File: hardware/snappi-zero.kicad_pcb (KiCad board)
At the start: 2 copper layers, 0 parts

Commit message: Place and route initial board.
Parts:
- added D1: A, LEDs:LED_1206, F.Cu at (210.0, 86.0)
- added D2: B, LEDs:LED_1206, F.Cu at (210.0, 90.5)
- added D3: C, LEDs:LED_1206, F.Cu at (210.0, 95.0)
- added G***: LOGO, CrumpPrintSymbols:Symbol_OSHW-Logo_12.5mm_NoText_Silkscreen, B.Cu at (202.0, 87.0)
- added G***: LOGO, ProjectSpecific:snappi-zero-logo, F.Cu at (199.5, 89.0)
- added P1: CONN_02X20, CrumpPrints:Raspberry_Pi_Zero, F.Cu at (148.5, 105.0)
- added R1: 10k, Resistors_SMD:R_0805_HandSoldering, F.Cu at (162.6, 101.6)
- added R2: 1k, Resistors_SMD:R_0805_HandSoldering, F.Cu at (200.0, 101.0)
- added R3: 1k, Resistors_SMD:R_0805_HandSoldering, F.Cu at (200.0, 103.5)
- added R4: 1k, Resistors_SMD:R_0805_HandSoldering, F.Cu at (200.0, 106.0)
- added U1: RF200, CrumpPrints:RF200_nosilk, F.Cu at (174.5, 95.0)
- added U2: SM220UF1, CrumpPrints:SM200_nosilk, F.Cu at (176.0, 93.5)
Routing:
- net GPIO_17: track 0.00 -> 64.5 mm, vias 0 -> 3
- net LED_C: track 0.00 -> 47.2 mm
- net LED_B: track 0.00 -> 38.6 mm
- net 3v3: track 0.00 -> 32.6 mm
- net LED_A: track 0.00 -> 32.3 mm
- net PI_TX: track 0.00 -> 32.0 mm, vias 0 -> 4
- net PI_RX: track 0.00 -> 27.0 mm
- net Net-(D1-Pad2): track 0.00 -> 17.9 mm
- net Net-(D2-Pad2): track 0.00 -> 16.3 mm
- net Net-(D3-Pad2): track 0.00 -> 15.7 mm
- net GND: track 0.00 -> 3.53 mm, vias 0 -> 2
- added copper zone on B.Cu, net GND
- added copper zone on F.Cu, net GND
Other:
- board outline added: 65 x 33 mm
- net class Default: clearance 0.254 -> 0.2032
- net class Thin added: clearance 0.1524, trace_width 0.2032, via_dia 0.889, via_drill 0.635
- rule trace_clearance: 0.254 -> 0.2032
- rule trace_min: 0.254 -> 0.1524
- board text added: "CC-BY-SA 4.0 @tylercrumpton"
- board text added: "SNAP Reset (Active Low): - Raspberry Pi BCM17 LED A: - RF GPIO_2 - SM GPIO_D3 LED B: - RF GPIO_1 - SM GPIO_D2 LED C: - RF GPIO_0 - SM GPIO_D1"
- board text added: "v1.0"

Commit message: Add TC logo and finalize PCB.
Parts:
- added svg2mod: G***, CrumpPrintSymbols:tc_30mm, F.Cu at (152.5, 85.5)
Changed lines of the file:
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@@
     (links 31)
     (no_connects 0)
-    (area 148.449999 74.949999 213.550001 108.050001)
+    (area 147.289372 73.0218 215.679391 116.278201)
     (thickness 1.6)
     (drawings 30)
     (tracks 106)
     (zones 0)
-    (modules 12)
+    (modules 13)
     (nets 92)
   )
@@
       (outputformat 1)
       (mirror false)
-      (drillshape 1)
+      (drillshape 0)
       (scaleselection 1)
       (outputdirectory ""))
@@
       (xy 2.253444 -4.352498)) (layer F.SilkS) (width 0.01))
   )
+  (module CrumpPrintSymbols:tc_30mm (layer F.Cu)
+    (at 152.5 85.5)
+    (descr "Imported from ../../../Dropbox/Vector Images/Other/tylercrumpton/tc.svg")
+    (tags svg2mod)
+    (attr smd)
+    (fp_text reference svg2mod (at 0 -5.231772) (layer F.SilkS) hide
+      (effects (font (thickness 0.3048)))
+    )
+    (fp_text value G*** (at 0 5.231772) (layer F.SilkS) hide
+      (effects (font (thickness 0.3048)))
+    )
+    (fp_poly (pts (xy 2.193664 1.877434) (xy 2.193664 -1.877434) (xy -2.193661 -1.877434) (xy -2.193661 1.877434)
+      (xy -0.80057 1.877434) (xy -0.80057 2.183772) (xy -2.499999 2.183772) (xy -2.499999 -2.183772)
+      (xy 2.499999 -2.183772) (xy 2.499999 2.183772) (xy 0.800528 2.183772) (xy 0.800528 1.877434)
+      (xy 2.193664 1.877434)) (layer F.SilkS) (width 0))
+    (fp_poly (pts (xy -0.686701 -0.454978) (xy -0.686701 0.8898) (xy -1.058682 0.8898) (xy -1.058682 -0.454978)
+      (xy -1.530792 -0.454978) (xy -1.530792 -0.776852) (xy -0.21459 -0.776852) (xy -0.21459 -0.454978)
+      (xy -0.686701 -0.454978)) (layer F.SilkS) (width 0))
+    (fp_poly (pts (xy 0.822581 0.56075) (xy 1.071754 0.506517) (xy 1.270841 0.343775) (xy 1.509259 0.589327)
+      (xy 1.308846 0.766865) (xy 1.08591 0.873352) (xy 0.84048 0.908837) (xy 0.598838 0.881819)
+      (xy 0.387421 0.80076) (xy 0.20623 0.665649) (xy 0.067795 0.489341) (xy -0.015267 0.284685)
+      (xy -0.042954 0.051661) (xy -0.01474 -0.181871) (xy 0.069908 -0.388124) (xy 0.211 -0.567098)
+      (xy 0.392861 -0.704846) (xy 0.59989 -0.787502) (xy 0.832078 -0.815056) (xy 1.09064 -0.780353)
+      (xy 1.31955 -0.676242) (xy 1.518799 -0.502723) (xy 1.287514 -0.240411) (xy 1.089604 -0.404947)
+      (xy 0.848795 -0.459792) (xy 0.654139 -0.425521) (xy 0.489942 -0.322684) (xy 0.378167 -0.161726)
+      (xy 0.340931 0.04689) (xy 0.376094 0.256414) (xy 0.481628 0.420053) (xy 0.637187 0.525587)
+      (xy 0.822581 0.56075)) (layer F.SilkS) (width 0))
+  )
   (gr_text "SNAP Reset (Active Low): \n - Raspberry Pi BCM17\nLED A:\n - RF GPIO_2\n - SM GPIO_D3\nLED B:\n - RF GPIO_1\n - SM GPIO_D2\nLED C:\n - RF GPIO_0\n - SM GPIO_D1" (at 184.5 95.5) (layer B.SilkS)

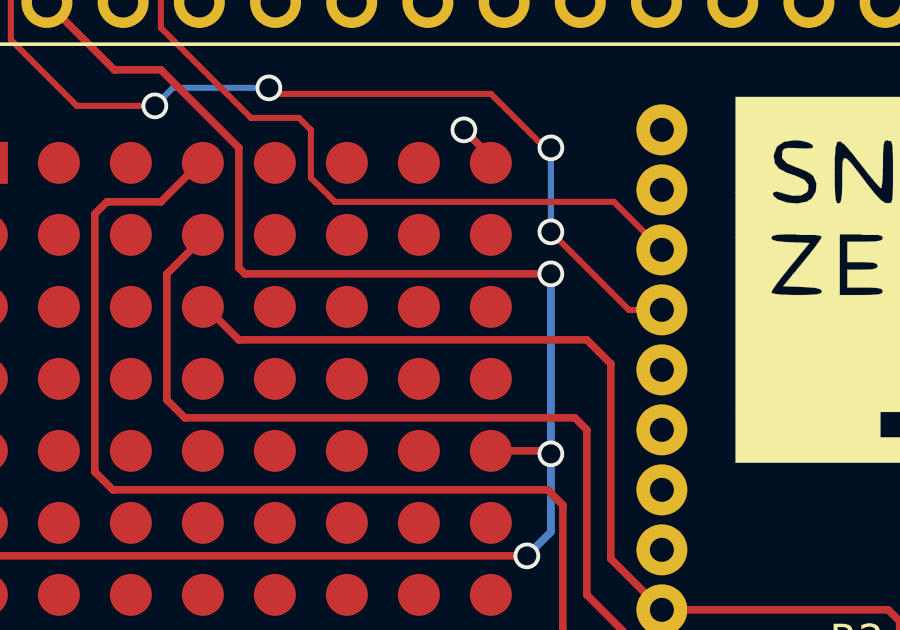
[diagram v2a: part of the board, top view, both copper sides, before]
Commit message: Fix missing TX/RX pins on SM modules.
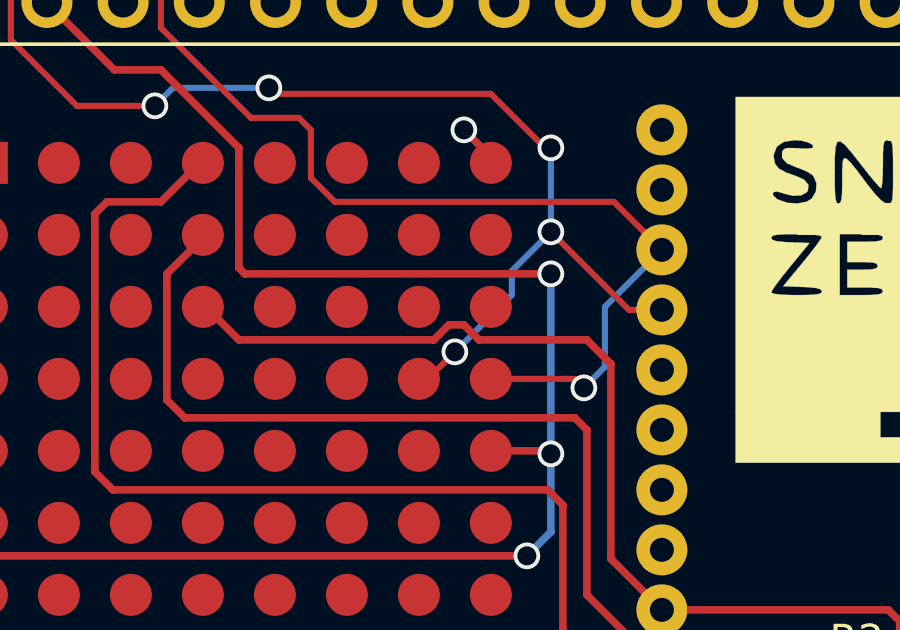
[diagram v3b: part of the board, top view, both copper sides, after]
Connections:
- P1 pad 13: Net-(P1-Pad13) -> (no net)
- P1 pad 14: Net-(P1-Pad14) -> (no net)
- P1 pad 15: Net-(P1-Pad15) -> (no net)
- P1 pad 16: Net-(P1-Pad16) -> (no net)
- P1 pad 17: Net-(P1-Pad17) -> (no net)
- P1 pad 18: Net-(P1-Pad18) -> (no net)
- P1 pad 19: Net-(P1-Pad19) -> (no net)
- P1 pad 2: Net-(P1-Pad2) -> (no net)
- P1 pad 20: Net-(P1-Pad20) -> (no net)
- P1 pad 21: Net-(P1-Pad21) -> (no net)
- P1 pad 22: Net-(P1-Pad22) -> (no net)
- P1 pad 23: Net-(P1-Pad23) -> (no net)
- P1 pad 24: Net-(P1-Pad24) -> (no net)
- P1 pad 25: Net-(P1-Pad25) -> (no net)
- P1 pad 26: Net-(P1-Pad26) -> (no net)
- P1 pad 27: Net-(P1-Pad27) -> (no net)
- P1 pad 28: Net-(P1-Pad28) -> (no net)
- P1 pad 29: Net-(P1-Pad29) -> (no net)
- P1 pad 3: Net-(P1-Pad3) -> (no net)
- P1 pad 30: Net-(P1-Pad30) -> (no net)
- P1 pad 31: Net-(P1-Pad31) -> (no net)
- P1 pad 32: Net-(P1-Pad32) -> (no net)
- P1 pad 33: Net-(P1-Pad33) -> (no net)
- P1 pad 34: Net-(P1-Pad34) -> (no net)
- P1 pad 35: Net-(P1-Pad35) -> (no net)
- P1 pad 36: Net-(P1-Pad36) -> (no net)
- P1 pad 37: Net-(P1-Pad37) -> (no net)
- P1 pad 38: Net-(P1-Pad38) -> (no net)
- P1 pad 39: Net-(P1-Pad39) -> (no net)
- P1 pad 4: Net-(P1-Pad4) -> (no net)
- P1 pad 40: Net-(P1-Pad40) -> (no net)
- P1 pad 5: Net-(P1-Pad5) -> (no net)
- P1 pad 6: Net-(P1-Pad6) -> (no net)
- P1 pad 7: Net-(P1-Pad7) -> (no net)
- P1 pad 8: Net-(P1-Pad8) -> (no net)
- U1 pad 11: Net-(U1-Pad11) -> (no net)
- U1 pad 12: Net-(U1-Pad12) -> (no net)
- U1 pad 13: Net-(U1-Pad13) -> (no net)
- U1 pad 14: Net-(U1-Pad14) -> (no net)
- U1 pad 15: Net-(U1-Pad15) -> (no net)
- U1 pad 16: Net-(U1-Pad16) -> (no net)
- U1 pad 17: Net-(U1-Pad17) -> (no net)
- U1 pad 18: Net-(U1-Pad18) -> (no net)
- U1 pad 19: Net-(U1-Pad19) -> (no net)
- U1 pad 20: Net-(U1-Pad20) -> (no net)
- U1 pad 22: Net-(U1-Pad22) -> (no net)
- U1 pad 5: Net-(U1-Pad5) -> (no net)
- U1 pad 6: Net-(U1-Pad6) -> (no net)
- U1 pad 7: Net-(U1-Pad7) -> (no net)
- U1 pad 8: Net-(U1-Pad8) -> (no net)
- U2 pad A4: Net-(U2-PadA4) -> (no net)
- U2 pad A5: Net-(U2-PadA5) -> (no net)
- U2 pad A6: Net-(U2-PadA6) -> (no net)
- U2 pad A7: Net-(U2-PadA7) -> (no net)
- U2 pad B1: Net-(U2-PadB1) -> (no net)
- U2 pad B2: Net-(U2-PadB2) -> (no net)
- U2 pad B3: Net-(U2-PadB3) -> (no net)
- U2 pad B4: Net-(U2-PadB4) -> (no net)
- U2 pad B6: Net-(U2-PadB6) -> (no net)
- U2 pad B7: Net-(U2-PadB7) -> (no net)
- U2 pad C1: Net-(U2-PadC1) -> (no net)
- U2 pad C2: Net-(U2-PadC2) -> (no net)
- U2 pad C3: Net-(U2-PadC3) -> (no net)
- U2 pad C4: Net-(U2-PadC4) -> (no net)
- U2 pad C5: Net-(U2-PadC5) -> (no net)
- U2 pad E1: Net-(U2-PadE1) -> (no net)
- U2 pad E2: Net-(U2-PadE2) -> (no net)
- U2 pad E3: Net-(U2-PadE3) -> (no net)
- U2 pad F1: Net-(U2-PadF1) -> (no net)
- U2 pad F2: Net-(U2-PadF2) -> (no net)
- U2 pad F3: Net-(U2-PadF3) -> (no net)
- U2 pad F4: Net-(U2-PadF4) -> (no net)
- U2 pad G1: Net-(U2-PadG1) -> (no net)
- U2 pad G2: Net-(U2-PadG2) -> (no net)
- U2 pad G3: Net-(U2-PadG3) -> (no net)
- U2 pad G4: Net-(U2-PadG4) -> PI_TX
- U2 pad G5: Net-(U2-PadG5) -> (no net)
- U2 pad H2: Net-(U2-PadH2) -> (no net)
- U2 pad H3: Net-(U2-PadH3) -> (no net)
- U2 pad H4: Net-(U2-PadH4) -> PI_RX
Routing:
- net PI_RX: track 27.0 -> 35.9 mm, vias 0 -> 1
- net PI_TX: track 32.0 -> 38.9 mm, vias 4 -> 5

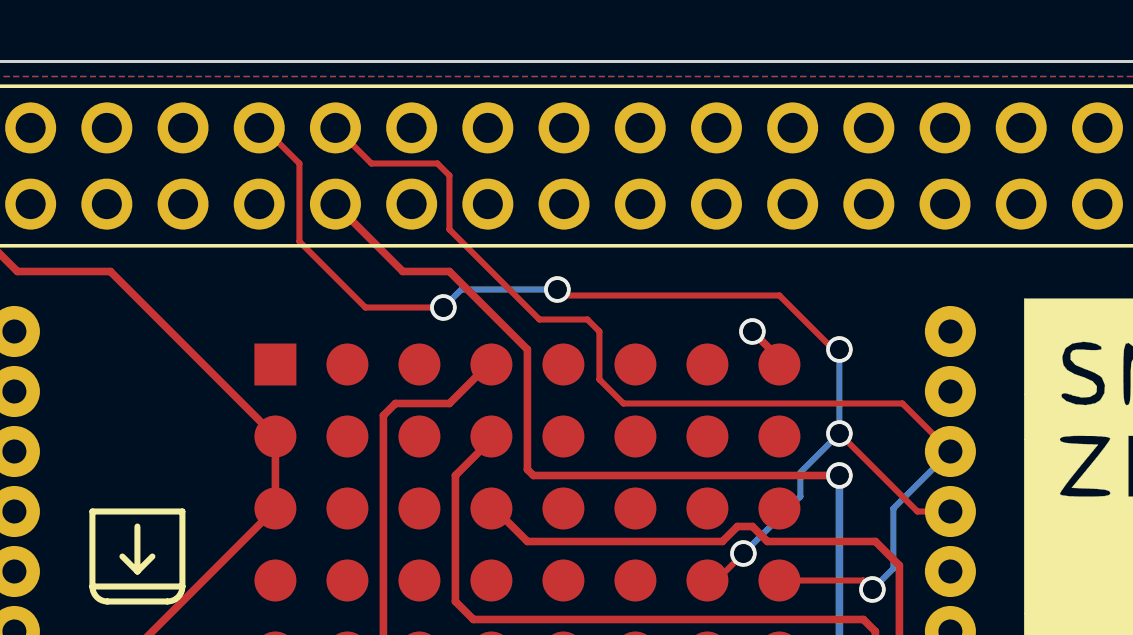
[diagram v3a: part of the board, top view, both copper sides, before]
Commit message: Fix Pi RX/TX pins.
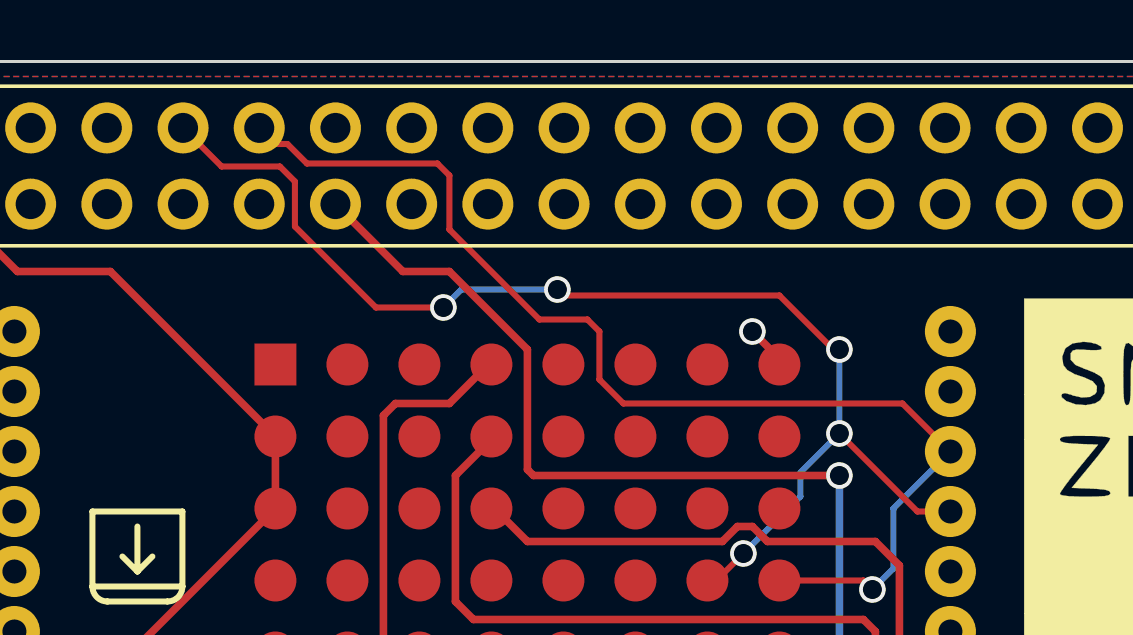
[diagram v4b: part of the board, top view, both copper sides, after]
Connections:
- P1 pad 10: PI_TX -> PI_RX
- P1 pad 12: PI_RX -> (no net)
- P1 pad 8: (no net) -> PI_TX
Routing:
- net PI_RX: track 35.9 -> 38.4 mm
- net PI_TX: track 38.9 -> 40.8 mm
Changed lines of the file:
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@@
     (thickness 1.6)
     (drawings 30)
-    (tracks 122)
+    (tracks 124)
     (zones 0)
     (modules 13)
@@
     (pad 6 thru_hole oval (at 13.48 -27.79 90) (size 1.7 1.7) (drill 1) (layers *.Cu *.Mask))
     (pad 7 thru_hole oval (at 16.02 -25.25 90) (size 1.7 1.7) (drill 1) (layers *.Cu *.Mask))
-    (pad 8 thru_hole oval (at 16.02 -27.79 90) (size 1.7 1.7) (drill 1) (layers *.Cu *.Mask))
+    (pad 8 thru_hole oval (at 16.02 -27.79 90) (size 1.7 1.7) (drill 1) (layers *.Cu *.Mask)
+      (net 6 PI_TX))
     (pad 9 thru_hole oval (at 18.56 -25.25 90) (size 1.7 1.7) (drill 1) (layers *.Cu *.Mask)
       (net 2 GND))
     (pad 10 thru_hole oval (at 18.56 -27.79 90) (size 1.7 1.7) (drill 1) (layers *.Cu *.Mask)
-      (net 6 PI_TX))
+      (net 8 PI_RX))
     (pad 11 thru_hole oval (at 21.1 -25.25 90) (size 1.7 1.7) (drill 1) (layers *.Cu *.Mask)
       (net 7 GPIO_17))
-    (pad 12 thru_hole oval (at 21.1 -27.79 90) (size 1.7 1.7) (drill 1) (layers *.Cu *.Mask)
-      (net 8 PI_RX))
+    (pad 12 thru_hole oval (at 21.1 -27.79 90) (size 1.7 1.7) (drill 1) (layers *.Cu *.Mask))
     (pad 13 thru_hole oval (at 23.64 -25.25 90) (size 1.7 1.7) (drill 1) (layers *.Cu *.Mask))
     (pad 14 thru_hole oval (at 23.64 -27.79 90) (size 1.7 1.7) (drill 1) (layers *.Cu *.Mask))
@@
   (segment (start 158.9 100) (end 162.31 100) (width 0.254) (layer F.Cu) (net 5))
   (segment (start 162.31 100) (end 162.56 100.25) (width 0.254) (layer F.Cu) (net 5))
-  (segment (start 185.1 88.7) (end 186.4 87.4) (width 0.2032) (layer B.Cu) (net 6))
-  (segment (start 185.1 89.5) (end 185.1 88.7) (width 0.2032) (layer B.Cu) (net 6))
-  (segment (start 183.2 91.4) (end 185.1 89.5) (width 0.2032) (layer B.Cu) (net 6))
-  (via (at 183.2 91.4) (size 0.889) (drill 0.635) (layers F.Cu B.Cu) (net 6))
-  (segment (start 182.3 92.3) (end 183.2 91.4) (width 0.2032) (layer F.Cu) (net 6))
-  (segment (start 182 92.3) (end 182.3 92.3) (width 0.2032) (layer F.Cu) (net 6))
-  (segment (start 167.0611 77.2136) (end 167.2136 77.2136) (width 0.2032) (layer F.Cu) (net 6))
-  (segment (start 167.2136 77.2136) (end 168.4 78.4) (width 0.2032) (layer F.Cu) (net 6))
-  (segment (start 168.4 78.4) (end 168.4 81) (width 0.2032) (layer F.Cu) (net 6))
-  (segment (start 168.4 81) (end 170.6 83.2) (width 0.2032) (layer F.Cu) (net 6))
-  (segment (start 170.6 83.2) (end 173.2 83.2) (width 0.2032) (layer F.Cu) (net 6))
+  (segment (start 173.2 83.2) (end 170.95 83.2) (width 0.2032) (layer F.Cu) (net 6))
+  (segment (start 186.4 87.4) (end 186.4 84.6) (width 0.2032) (layer B.Cu) (net 6))
+  (via (at 186.4 84.6) (size 0.889) (drill 0.635) (layers F.Cu B.Cu) (net 6))
+  (segment (start 184.4 82.8) (end 186.2 84.6) (width 0.2032) (layer F.Cu) (net 6))
   (via (at 173.2 83.2) (size 0.889) (drill 0.635) (layers F.Cu B.Cu) (net 6))
   (segment (start 173.2 83.2) (end 173.8 82.6) (width 0.2032) (layer B.Cu) (net 6))
@@
   (segment (start 177 82.6) (end 177.2 82.8) (width 0.2032) (layer F.Cu) (net 6))
   (segment (start 177.2 82.8) (end 184.4 82.8) (width 0.2032) (layer F.Cu) (net 6))
-  (segment (start 184.4 82.8) (end 186.2 84.6) (width 0.2032) (layer F.Cu) (net 6))
   (segment (start 186.2 84.6) (end 186.4 84.6) (width 0.2032) (layer F.Cu) (net 6))
-  (via (at 186.4 84.6) (size 0.889) (drill 0.635) (layers F.Cu B.Cu) (net 6))
-  (segment (start 186.4 84.6) (end 186.4 87.4) (width 0.2032) (layer B.Cu) (net 6))
+  (segment (start 165.8075 78.5) (end 164.5211 77.2136) (width 0.2032) (layer F.Cu) (net 6))
+  (segment (start 167.75 78.5) (end 165.8075 78.5) (width 0.2032) (layer F.Cu) (net 6))
+  (segment (start 168.25 79) (end 167.75 78.5) (width 0.2032) (layer F.Cu) (net 6))
+  (segment (start 168.25 80.5) (end 168.25 79) (width 0.2032) (layer F.Cu) (net 6))
+  (segment (start 170.95 83.2) (end 168.25 80.5) (width 0.2032) (layer F.Cu) (net 6))
+  (segment (start 183.2 91.4) (end 185.1 89.5) (width 0.2032) (layer B.Cu) (net 6))
+  (via (at 183.2 91.4) (size 0.889) (drill 0.635) (layers F.Cu B.Cu) (net 6))
+  (segment (start 182.3 92.3) (end 183.2 91.4) (width 0.2032) (layer F.Cu) (net 6))
+  (segment (start 182 92.3) (end 182.3 92.3) (width 0.2032) (layer F.Cu) (net 6))
+  (segment (start 189 90) (end 190.1 90) (width 0.2032) (layer F.Cu) (net 6))
+  (segment (start 185.1 88.7) (end 186.4 87.4) (width 0.2032) (layer B.Cu) (net 6))
+  (segment (start 185.1 89.5) (end 185.1 88.7) (width 0.2032) (layer B.Cu) (net 6))
   (via (at 186.4 87.4) (size 0.889) (drill 0.635) (layers F.Cu B.Cu) (net 6))
   (segment (start 186.4 87.4) (end 189 90) (width 0.2032) (layer F.Cu) (net 6))
-  (segment (start 189 90) (end 190.1 90) (width 0.2032) (layer F.Cu) (net 6))
   (segment (start 186.4 94.8) (end 186.4 88.8) (width 0.254) (layer B.Cu) (net 7))
   (segment (start 173.4 82) (end 171.8475 82) (width 0.254) (layer F.Cu) (net 7))
@@
   (segment (start 158.9 104) (end 161.51 104) (width 0.254) (layer F.Cu) (net 7))
   (segment (start 161.51 104) (end 162.56 102.95) (width 0.254) (layer F.Cu) (net 7))
-  (segment (start 184.4 92.3) (end 187.2 92.3) (width 0.2032) (layer F.Cu) (net 8))
-  (segment (start 188.2 89.9) (end 190.1 88) (width 0.2032) (layer B.Cu) (net 8))
-  (segment (start 188.2 91.9) (end 188.2 89.9) (width 0.2032) (layer B.Cu) (net 8))
-  (segment (start 187.5 92.6) (end 188.2 91.9) (width 0.2032) (layer B.Cu) (net 8))
-  (via (at 187.5 92.6) (size 0.889) (drill 0.635) (layers F.Cu B.Cu) (net 8))
-  (segment (start 187.2 92.3) (end 187.5 92.6) (width 0.2032) (layer F.Cu) (net 8))
-  (segment (start 169.6011 77.2136) (end 169.6136 77.2136) (width 0.2032) (layer F.Cu) (net 8))
-  (segment (start 169.6136 77.2136) (end 170.8 78.4) (width 0.2032) (layer F.Cu) (net 8))
-  (segment (start 170.8 78.4) (end 173 78.4) (width 0.2032) (layer F.Cu) (net 8))
+  (segment (start 173 78.4) (end 168.65 78.4) (width 0.2032) (layer F.Cu) (net 8))
   (segment (start 173 78.4) (end 173.4 78.8) (width 0.2032) (layer F.Cu) (net 8))
   (segment (start 173.4 78.8) (end 173.4 80.6) (width 0.2032) (layer F.Cu) (net 8))
@@
   (segment (start 178.4 85.6) (end 179.2 86.4) (width 0.2032) (layer F.Cu) (net 8))
   (segment (start 179.2 86.4) (end 188.5 86.4) (width 0.2032) (layer F.Cu) (net 8))
-  (segment (start 188.5 86.4) (end 190.1 88) (width 0.2032) (layer F.Cu) (net 8))
+  (segment (start 190.1 88) (end 188.5 86.4) (width 0.2032) (layer F.Cu) (net 8))
+  (segment (start 168 77.75) (end 167.5975 77.75) (width 0.2032) (layer F.Cu) (net 8))
+  (segment (start 168.65 78.4) (end 168 77.75) (width 0.2032) (layer F.Cu) (net 8))
+  (segment (start 167.5975 77.75) (end 167.0611 77.2136) (width 0.2032) (layer F.Cu) (net 8))
+  (segment (start 184.4 92.3) (end 187.2 92.3) (width 0.2032) (layer F.Cu) (net 8))
+  (segment (start 188.2 89.9) (end 190.1 88) (width 0.2032) (layer B.Cu) (net 8))
+  (segment (start 188.2 91.9) (end 188.2 89.9) (width 0.2032) (layer B.Cu) (net 8))
+  (segment (start 187.5 92.6) (end 188.2 91.9) (width 0.2032) (layer B.Cu) (net 8))
+  (via (at 187.5 92.6) (size 0.889) (drill 0.635) (layers F.Cu B.Cu) (net 8))
+  (segment (start 187.2 92.3) (end 187.5 92.6) (width 0.2032) (layer F.Cu) (net 8))
   (segment (start 190.1 100) (end 197.65 100) (width 0.254) (layer F.Cu) (net 9))
   (segment (start 174.8 89.9) (end 174.9 89.9) (width 0.254) (layer F.Cu) (net 9))
